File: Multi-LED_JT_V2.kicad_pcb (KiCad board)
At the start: 2 copper layers, 54.1 x 14.5 mm, 12 parts, among them Q1 BC817-25, SW1 SW_DPDT

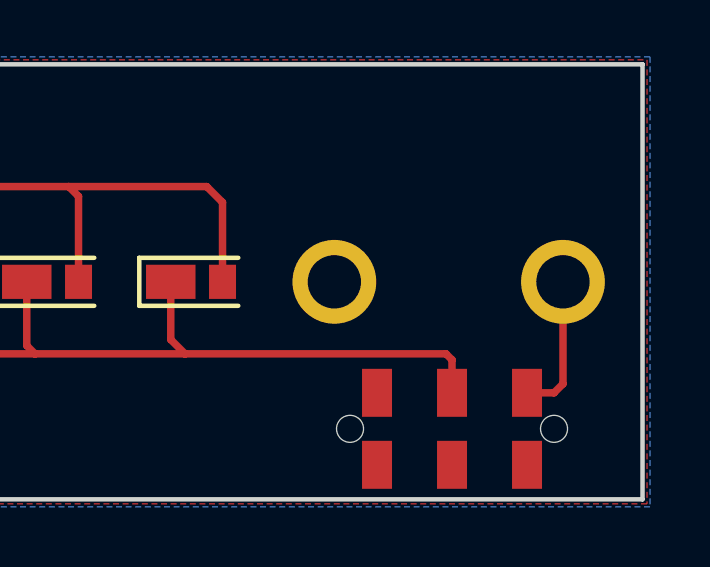
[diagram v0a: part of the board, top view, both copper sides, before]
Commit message: add to f.SilkS ON with arrow indicator
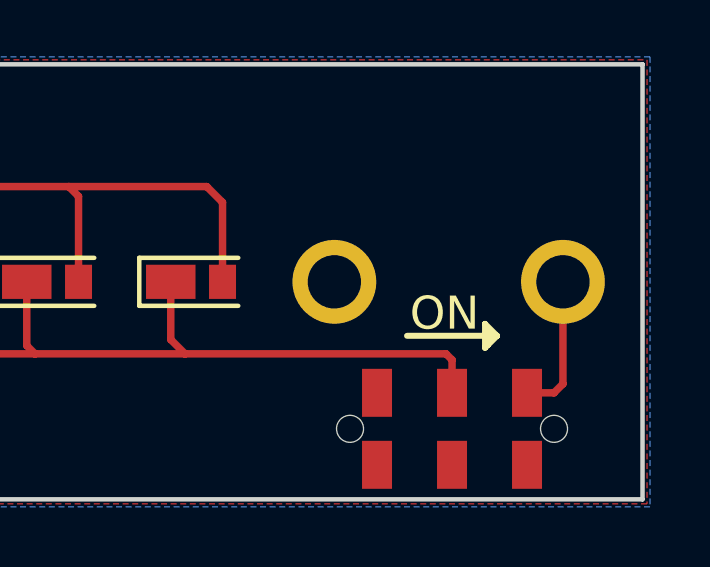
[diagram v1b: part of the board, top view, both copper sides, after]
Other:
- board text added: "ON"
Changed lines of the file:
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@@
     (links 19)
     (no_connects 0)
-    (area 185.3 104.925 239.900001 120.400001)
+    (area 185.474999 105.574999 239.725001 120.225001)
     (thickness 1.6)
-    (drawings 6)
+    (drawings 13)
     (tracks 64)
     (zones 0)
@@
   (module lib_fp:DPDT_JS202011JAQN (layer F.Cu)
     (at 233.3 117.8)
-    (fp_text reference SW1 (at 0.1 -2.8) (layer F.SilkS) hide
+    (fp_text reference SW1 (at 0 -1.25) (layer F.SilkS) hide
       (effects (font (size 1 1) (thickness 0.15)))
     )
@@
     (pad "" np_thru_hole circle (at 3.4 0) (size 0.9 0.9) (drill 0.9) (layers *.Cu *.Mask))
   )
+  (gr_line (start 234.5 114.45) (end 234.45 114.45) (angle 90) (layer F.SilkS) (width 0.2))
+  (gr_line (start 234.5 115) (end 234.5 114.45) (angle 90) (layer F.SilkS) (width 0.2))
+  (gr_line (start 234.4 114.3) (end 234.4 115.1) (angle 90) (layer F.SilkS) (width 0.2))
+  (gr_line (start 234.8 114.7) (end 234.4 114.3) (angle 90) (layer F.SilkS) (width 0.2))
+  (gr_line (start 234.8 114.7) (end 234.4 115.1) (angle 90) (layer F.SilkS) (width 0.2))
+  (gr_text ON (at 233.05 113.95) (layer F.SilkS)
+    (effects (font (size 1.1 1.1) (thickness 0.17)))
+  )
+  (gr_line (start 234.8 114.7) (end 231.8 114.7) (angle 90) (layer F.SilkS) (width 0.2))
   (gr_text "1.5V AA (LR6)" (at 212.8 117.5) (layer B.SilkS)
     (effects (font (size 1 1) (thickness 0.1)) (justify mirror))
